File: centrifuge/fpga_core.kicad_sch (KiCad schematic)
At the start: 2 parts

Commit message: Made initial pin map of SRAM-FPGA and possible routing
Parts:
- U1: renamed from U?; footprint (none) -> Package_BGA:Xilinx_FTG256
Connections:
- net GND: now reaches U1.A1 (GND)
- net GND: now also U1.A11 (GND), U1.B8 (GND), U1.C15 (GND), U1.C5 (GND), U1.D12 (GND), U1.D2 (GND), U1.E9 (GND), U1.F10 (GND), U1.F16 (GND), U1.F6 (GND), U1.G13 (GND), U1.G3 (GND), U1.G9 (GND), U1.H6 (GND), U1.J11 (GND), U1.J9 (GND), U1.K14 (GND), U1.K4 (GND), U1.K6 (GND), U1.L1 (GND), U1.L11 (GND), U1.M8 (GND), U1.N15 (GND), U1.N5 (GND), U1.P12 (GND), U1.P2 (GND), U1.R9 (GND), U1.T16 (GND), U1.T6 (GND)
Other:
- removed sheet dram
- sheet config_dram ports: added CCLK; removed none
- sheet pwr_jtag ports: added CCLK, CONFIG_DONE, PROGRAM_B, VCCO_0; removed none

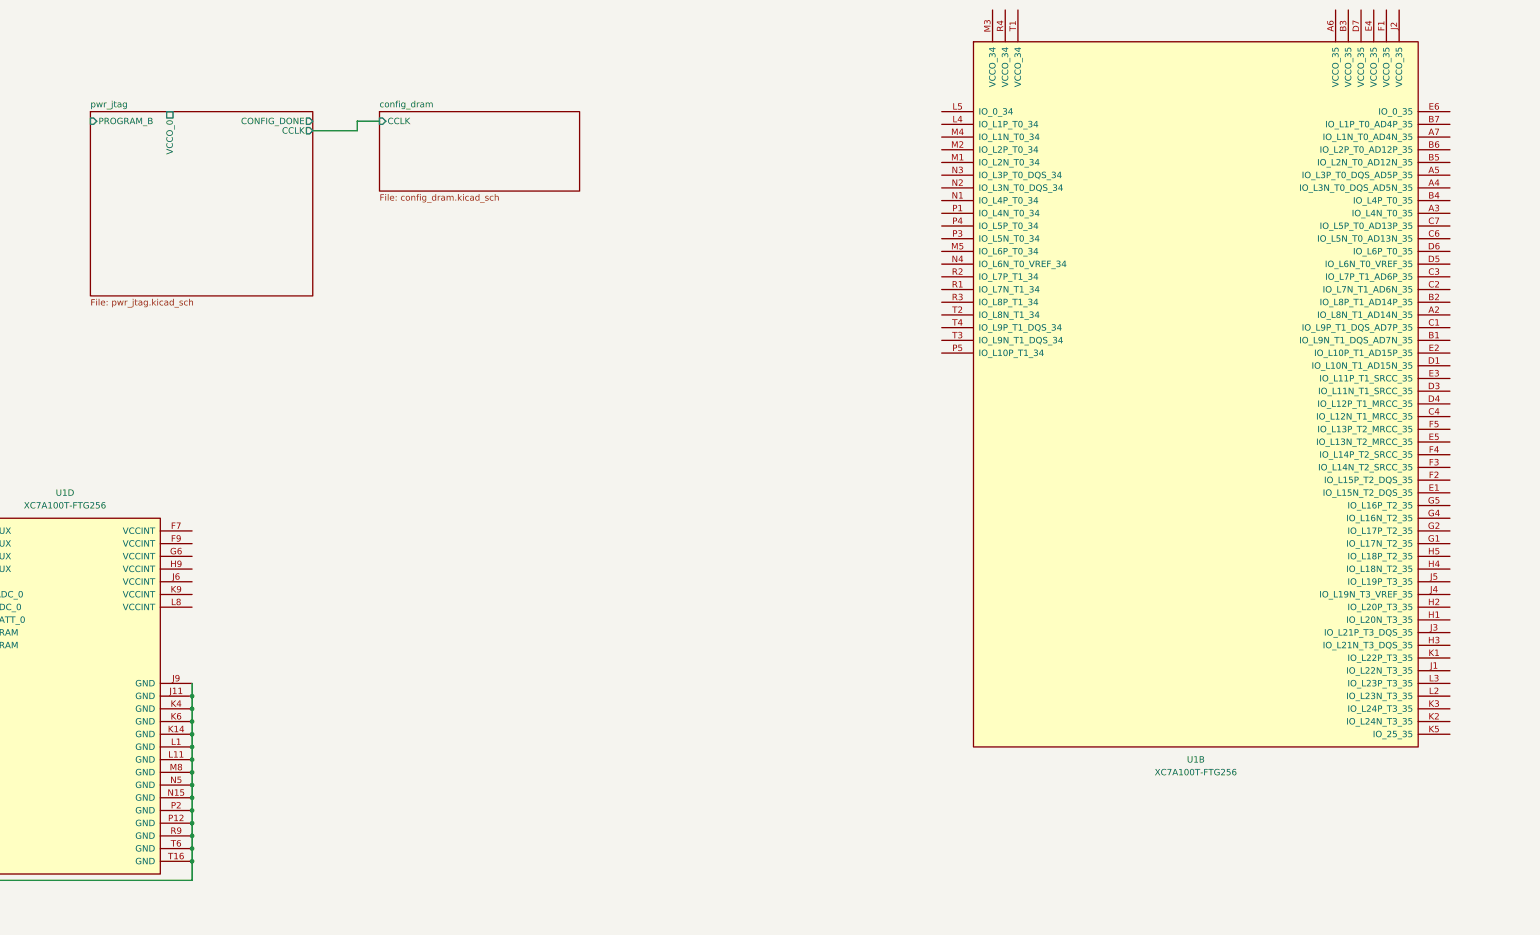
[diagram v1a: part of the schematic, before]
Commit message: Completed majority of schematic, need to add decoupling but otherwise mostly ready
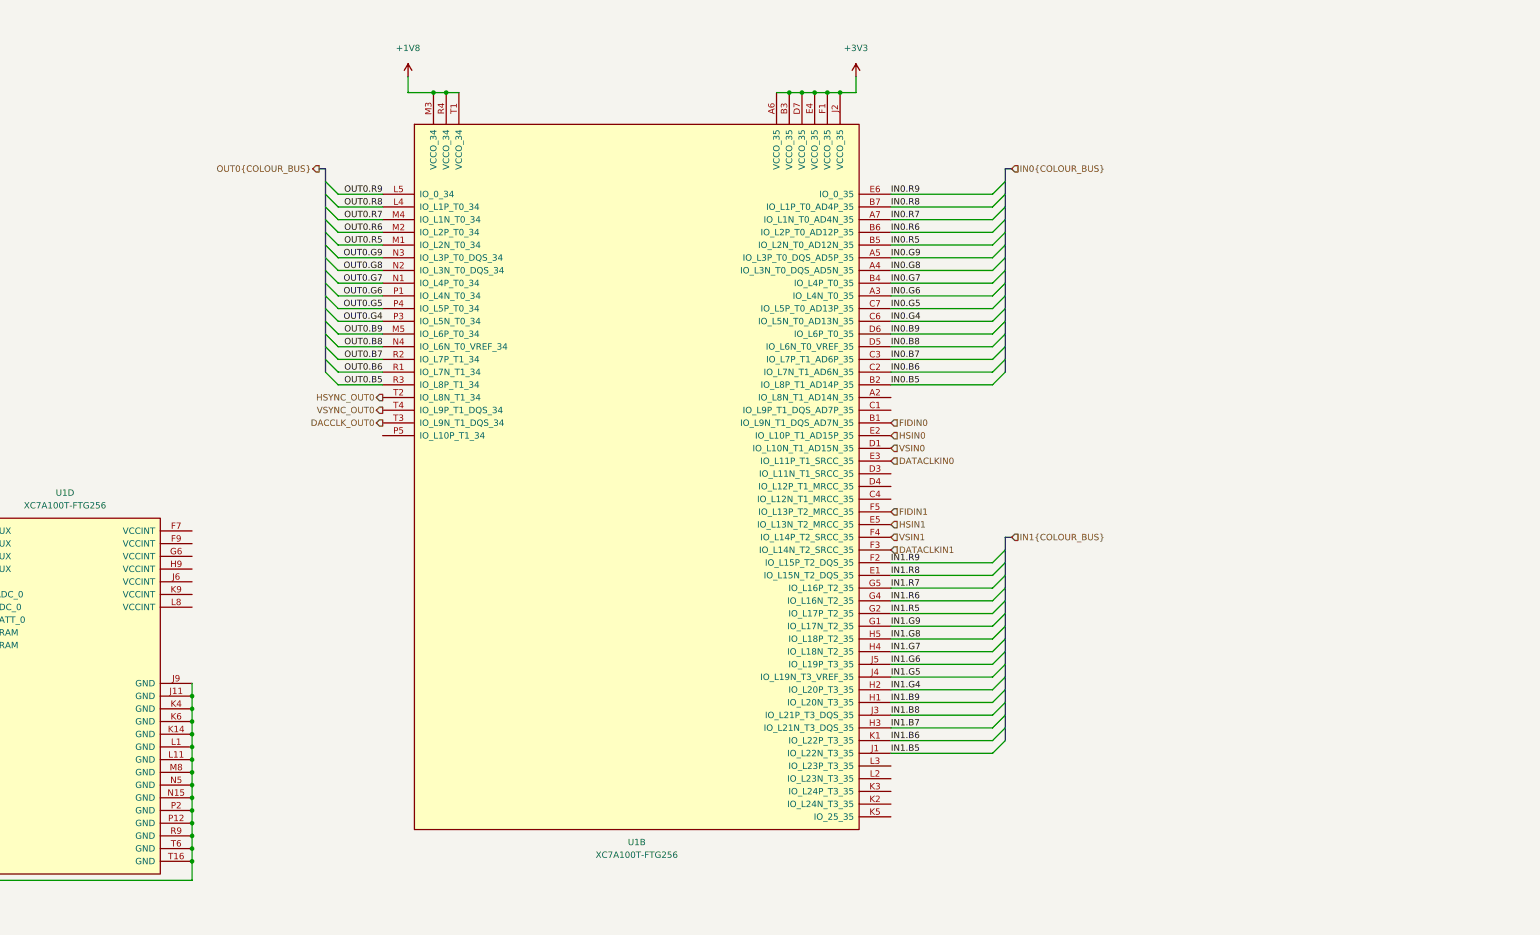
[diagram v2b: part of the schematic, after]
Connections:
- net IN0.G6: now reaches U1.A3 (IO_L4N_T0_35)
- net IN0.G8: now reaches U1.A4 (IO_L3N_T0_DQS_AD5N_35)
- net IN0.G9: now reaches U1.A5 (IO_L3P_T0_DQS_AD5P_35)
- net +3V3: now reaches U1.A6 (VCCO_35)
- net +3V3: now also U1.B3 (VCCO_35), U1.D7 (VCCO_35), U1.E4 (VCCO_35), U1.F1 (VCCO_35), U1.J2 (VCCO_35)
- net IN0.R7: now reaches U1.A7 (IO_L1N_T0_AD4N_35)
- net FIDIN0: now reaches U1.B1 (IO_L9N_T1_DQS_AD7N_35)
- net IN0.B5: now reaches U1.B2 (IO_L8P_T1_AD14P_35)
- net IN0.G7: now reaches U1.B4 (IO_L4P_T0_35)
- net IN0.R5: now reaches U1.B5 (IO_L2N_T0_AD12N_35)
- net IN0.R6: now reaches U1.B6 (IO_L2P_T0_AD12P_35)
- net IN0.R8: now reaches U1.B7 (IO_L1P_T0_AD4P_35)
- net IN0.B6: now reaches U1.C2 (IO_L7N_T1_AD6N_35)
- net IN0.B7: now reaches U1.C3 (IO_L7P_T1_AD6P_35)
- net IN0.G4: now reaches U1.C6 (IO_L5N_T0_AD13N_35)
- net IN0.G5: now reaches U1.C7 (IO_L5P_T0_AD13P_35)
- net VSIN0: now reaches U1.D1 (IO_L10N_T1_AD15N_35)
- net IN0.B8: now reaches U1.D5 (IO_L6N_T0_VREF_35)
- net IN0.B9: now reaches U1.D6 (IO_L6P_T0_35)
- net IN1.R8: now reaches U1.E1 (IO_L15N_T2_DQS_35)
- net HSIN0: now reaches U1.E2 (IO_L10P_T1_AD15P_35)
- net DATACLKIN0: now reaches U1.E3 (IO_L11P_T1_SRCC_35)
- net HSIN1: now reaches U1.E5 (IO_L13N_T2_MRCC_35)
- net IN0.R9: now reaches U1.E6 (IO_0_35)
- net IN1.R9: now reaches U1.F2 (IO_L15P_T2_DQS_35)
- net DATACLKIN1: now reaches U1.F3 (IO_L14N_T2_SRCC_35)
- net VSIN1: now reaches U1.F4 (IO_L14P_T2_SRCC_35)
- net FIDIN1: now reaches U1.F5 (IO_L13P_T2_MRCC_35)
- net IN1.G9: now reaches U1.G1 (IO_L17N_T2_35)
- net IN1.R5: now reaches U1.G2 (IO_L17P_T2_35)
- net IN1.R6: now reaches U1.G4 (IO_L16N_T2_35)
- net IN1.R7: now reaches U1.G5 (IO_L16P_T2_35)
- net IN1.B9: now reaches U1.H1 (IO_L20N_T3_35)
- net IN1.G4: now reaches U1.H2 (IO_L20P_T3_35)
- net IN1.B7: now reaches U1.H3 (IO_L21N_T3_DQS_35)
- net IN1.G7: now reaches U1.H4 (IO_L18N_T2_35)
- net IN1.G8: now reaches U1.H5 (IO_L18P_T2_35)
- net IN1.B5: now reaches U1.J1 (IO_L22N_T3_35)
- net IN1.B8: now reaches U1.J3 (IO_L21P_T3_DQS_35)
- net IN1.G5: now reaches U1.J4 (IO_L19N_T3_VREF_35)
- net IN1.G6: now reaches U1.J5 (IO_L19P_T3_35)
- net IN1.B6: now reaches U1.K1 (IO_L22P_T3_35)
- net OUT0.R8: now reaches U1.L4 (IO_L1P_T0_34)
- net OUT0.R9: now reaches U1.L5 (IO_0_34)
- net OUT0.R5: now reaches U1.M1 (IO_L2N_T0_34)
- net OUT0.R6: now reaches U1.M2 (IO_L2P_T0_34)
- net +1V8: now reaches U1.M3 (VCCO_34)
- net +1V8: now also U1.R4 (VCCO_34), U1.T1 (VCCO_34)
- net OUT0.R7: now reaches U1.M4 (IO_L1N_T0_34)
- net OUT0.B9: now reaches U1.M5 (IO_L6P_T0_34)
- net OUT0.G7: now reaches U1.N1 (IO_L4P_T0_34)
- net OUT0.G8: now reaches U1.N2 (IO_L3N_T0_DQS_34)
- net OUT0.G9: now reaches U1.N3 (IO_L3P_T0_DQS_34)
- net OUT0.B8: now reaches U1.N4 (IO_L6N_T0_VREF_34)
- net OUT0.G6: now reaches U1.P1 (IO_L4N_T0_34)
- net OUT0.G4: now reaches U1.P3 (IO_L5N_T0_34)
- net OUT0.G5: now reaches U1.P4 (IO_L5P_T0_34)
- net OUT0.B6: now reaches U1.R1 (IO_L7N_T1_34)
- net OUT0.B7: now reaches U1.R2 (IO_L7P_T1_34)
- net OUT0.B5: now reaches U1.R3 (IO_L8P_T1_34)
- net HSYNC_OUT0: now reaches U1.T2 (IO_L8N_T1_34)
- net DACCLK_OUT0: now reaches U1.T3 (IO_L9N_T1_DQS_34)
- net VSYNC_OUT0: now reaches U1.T4 (IO_L9P_T1_DQS_34)
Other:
- removed sheet config_dram
- removed sheet pwr_jtag
- title: VGA Centrifuge FPGA board -> VGA Centrifuge
- moved on the sheet: U1B

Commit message: FPGA PCB design completed
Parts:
- removed unit 4 of U1
- added C100, C101, C102, C103, C96, C97, C98, C99: 470n, Capacitor_SMD:C_0603_1608Metric_Pad1.08x0.95mm_HandSolder, symbol Device:C_Small
- added C104, C105, C106, C107: 4.7u, Capacitor_SMD:C_0805_2012Metric_Pad1.18x1.45mm_HandSolder, symbol Device:C_Small
- added C108: 47u X5R/X7R, Capacitor_SMD:C_1210_3225Metric_Pad1.33x2.70mm_HandSolder, symbol Device:C_Small
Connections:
- net +1V8: now also C100.1, C102.1, C104.1, C106.1, C108.1, C96.1, C98.1
- net +3V3: now also C101.1, C103.1, C105.1, C107.1, C97.1, C99.1
- net DACCLK_OUT0: now also U1.L4 (IO_L1P_T0_34); no longer U1.T3 (IO_L9N_T1_DQS_34)
- net DATACLKIN0: now also U1.E5 (IO_L13N_T2_MRCC_35); no longer U1.E3 (IO_L11P_T1_SRCC_35)
- net DATACLKIN1: now also U1.F5 (IO_L13P_T2_MRCC_35); no longer U1.F3 (IO_L14N_T2_SRCC_35)
- net FIDIN0: now also U1.E1 (IO_L15N_T2_DQS_35); no longer U1.B1 (IO_L9N_T1_DQS_AD7N_35)
- net FIDIN1: now also U1.J4 (IO_L19N_T3_VREF_35); no longer U1.F5 (IO_L13P_T2_MRCC_35)
- net GND: now also C100.2, C101.2, C102.2, C103.2, C104.2, C105.2, C106.2, C107.2, C108.2, C96.2, C97.2, C98.2, C99.2
- net HSIN0: now also U1.D1 (IO_L10N_T1_AD15N_35); no longer U1.E2 (IO_L10P_T1_AD15P_35)
- net HSIN1: now also U1.K3 (IO_L24P_T3_35); no longer U1.E5 (IO_L13N_T2_MRCC_35)
- net HSYNC_OUT0: now also U1.L5 (IO_0_34); no longer U1.T2 (IO_L8N_T1_34)
- net IN0.B5: now also U1.A2 (IO_L8N_T1_AD14N_35); no longer U1.B2 (IO_L8P_T1_AD14P_35)
- net IN0.B6: now also U1.B2 (IO_L8P_T1_AD14P_35); no longer U1.C2 (IO_L7N_T1_AD6N_35)
- net IN0.B7: now also U1.B1 (IO_L9N_T1_DQS_AD7N_35); no longer U1.C3 (IO_L7P_T1_AD6P_35)
- net IN0.B8: now also U1.C2 (IO_L7N_T1_AD6N_35); no longer U1.D5 (IO_L6N_T0_VREF_35)
- net IN0.B9: now also U1.C1 (IO_L9P_T1_DQS_AD7P_35); no longer U1.D6 (IO_L6P_T0_35)
- net IN0.G4: now also U1.D3 (IO_L11N_T1_SRCC_35); no longer U1.C6 (IO_L5N_T0_AD13N_35)
- net IN0.G5: now also U1.E3 (IO_L11P_T1_SRCC_35); no longer U1.C7 (IO_L5P_T0_AD13P_35)
- net IN0.G6: now also U1.B4 (IO_L4P_T0_35); no longer U1.A3 (IO_L4N_T0_35)
- net IN0.G7: now also U1.A4 (IO_L3N_T0_DQS_AD5N_35); no longer U1.B4 (IO_L4P_T0_35)
- net IN0.G8: now also U1.A3 (IO_L4N_T0_35); no longer U1.A4 (IO_L3N_T0_DQS_AD5N_35)
- net IN0.G9: now also U1.C3 (IO_L7P_T1_AD6P_35); no longer U1.A5 (IO_L3P_T0_DQS_AD5P_35)
- net IN0.R5: now also U1.B7 (IO_L1P_T0_AD4P_35); no longer U1.B5 (IO_L2N_T0_AD12N_35)
- net IN0.R6: now also U1.A7 (IO_L1N_T0_AD4N_35); no longer U1.B6 (IO_L2P_T0_AD12P_35)
- net IN0.R7: now also U1.B6 (IO_L2P_T0_AD12P_35); no longer U1.A7 (IO_L1N_T0_AD4N_35)
- net IN0.R8: now also U1.B5 (IO_L2N_T0_AD12N_35); no longer U1.B7 (IO_L1P_T0_AD4P_35)
- net IN0.R9: now also U1.A5 (IO_L3P_T0_DQS_AD5P_35); no longer U1.E6 (IO_0_35)
- net IN1.B6: now also U1.K2 (IO_L24N_T3_35); no longer U1.K1 (IO_L22P_T3_35)
- net IN1.B7: now also U1.K1 (IO_L22P_T3_35); no longer U1.H3 (IO_L21N_T3_DQS_35)
- net IN1.B8: now also U1.L3 (IO_L23P_T3_35); no longer U1.J3 (IO_L21P_T3_DQS_35)
- net IN1.B9: now also U1.L2 (IO_L23N_T3_35); no longer U1.H1 (IO_L20N_T3_35)
- net IN1.G4: now also U1.F2 (IO_L15P_T2_DQS_35); no longer U1.H2 (IO_L20P_T3_35)
- net IN1.G5: now also U1.G2 (IO_L17P_T2_35); no longer U1.J4 (IO_L19N_T3_VREF_35)
- net IN1.G6: now also U1.G1 (IO_L17N_T2_35); no longer U1.J5 (IO_L19P_T3_35)
- net IN1.G7: now also U1.H2 (IO_L20P_T3_35); no longer U1.H4 (IO_L18N_T2_35)
- net IN1.G8: now also U1.H1 (IO_L20N_T3_35); no longer U1.H5 (IO_L18P_T2_35)
- net IN1.G9: now also U1.J3 (IO_L21P_T3_DQS_35); no longer U1.G1 (IO_L17N_T2_35)
- net IN1.R5: now also U1.H4 (IO_L18N_T2_35); no longer U1.G2 (IO_L17P_T2_35)
- net IN1.R6: now also U1.H5 (IO_L18P_T2_35); no longer U1.G4 (IO_L16N_T2_35)
- net IN1.R7: now also U1.H3 (IO_L21N_T3_DQS_35); no longer U1.G5 (IO_L16P_T2_35)
- net IN1.R8: now also U1.G4 (IO_L16N_T2_35); no longer U1.E1 (IO_L15N_T2_DQS_35)
- net IN1.R9: now also U1.F4 (IO_L14P_T2_SRCC_35); no longer U1.F2 (IO_L15P_T2_DQS_35)
- net OUT0.B5: now also U1.R1 (IO_L7N_T1_34); no longer U1.R3 (IO_L8P_T1_34)
- net OUT0.B6: now also U1.R2 (IO_L7P_T1_34); no longer U1.R1 (IO_L7N_T1_34)
- net OUT0.B7: now also U1.T2 (IO_L8N_T1_34); no longer U1.R2 (IO_L7P_T1_34)
- net OUT0.B8: now also U1.R3 (IO_L8P_T1_34); no longer U1.N4 (IO_L6N_T0_VREF_34)
- net OUT0.B9: now also U1.T3 (IO_L9N_T1_DQS_34); no longer U1.M5 (IO_L6P_T0_34)
- net OUT0.G4: now also U1.M5 (IO_L6P_T0_34); no longer U1.P3 (IO_L5N_T0_34)
- net OUT0.G6: now also U1.N4 (IO_L6N_T0_VREF_34); no longer U1.P1 (IO_L4N_T0_34)
- net OUT0.G7: now also U1.P3 (IO_L5N_T0_34); no longer U1.N1 (IO_L4P_T0_34)
- net OUT0.G8: now also U1.M4 (IO_L1N_T0_34); no longer U1.N2 (IO_L3N_T0_DQS_34)
- net OUT0.R5: now also U1.P1 (IO_L4N_T0_34); no longer U1.M1 (IO_L2N_T0_34)
- net OUT0.R6: now also U1.N2 (IO_L3N_T0_DQS_34); no longer U1.M2 (IO_L2P_T0_34)
- net OUT0.R7: now also U1.N1 (IO_L4P_T0_34); no longer U1.M4 (IO_L1N_T0_34)
- net OUT0.R8: now also U1.M2 (IO_L2P_T0_34); no longer U1.L4 (IO_L1P_T0_34)
- net OUT0.R9: now also U1.M1 (IO_L2N_T0_34); no longer U1.L5 (IO_0_34)
- net VSIN0: now also U1.E2 (IO_L10P_T1_AD15P_35); no longer U1.D1 (IO_L10N_T1_AD15N_35)
- net VSIN1: now also U1.J5 (IO_L19P_T3_35); no longer U1.F4 (IO_L14P_T2_SRCC_35)
- net AUXIO18: now reaches U1.C4 (IO_L12N_T1_MRCC_35)
- net AUXIO19: now reaches U1.D4 (IO_L12P_T1_MRCC_35)
- net AUXIO17L: now reaches U1.P5 (IO_L10P_T1_34)
- new net AUXIO20: U1.D5 (IO_L6N_T0_VREF_35)
- new net AUXIO21: U1.D6 (IO_L6P_T0_35)
- new net AUXIO22: U1.C6 (IO_L5N_T0_AD13N_35)
- new net AUXIO23: U1.C7 (IO_L5P_T0_AD13P_35)
- new net AUXIO24: U1.E6 (IO_0_35)
- no-connect marks 0 -> 3
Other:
- moved on the sheet: U1B
